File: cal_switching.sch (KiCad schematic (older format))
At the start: 2 parts, among them U20 TMUX6111PWR, U21 TMUX6111PWR

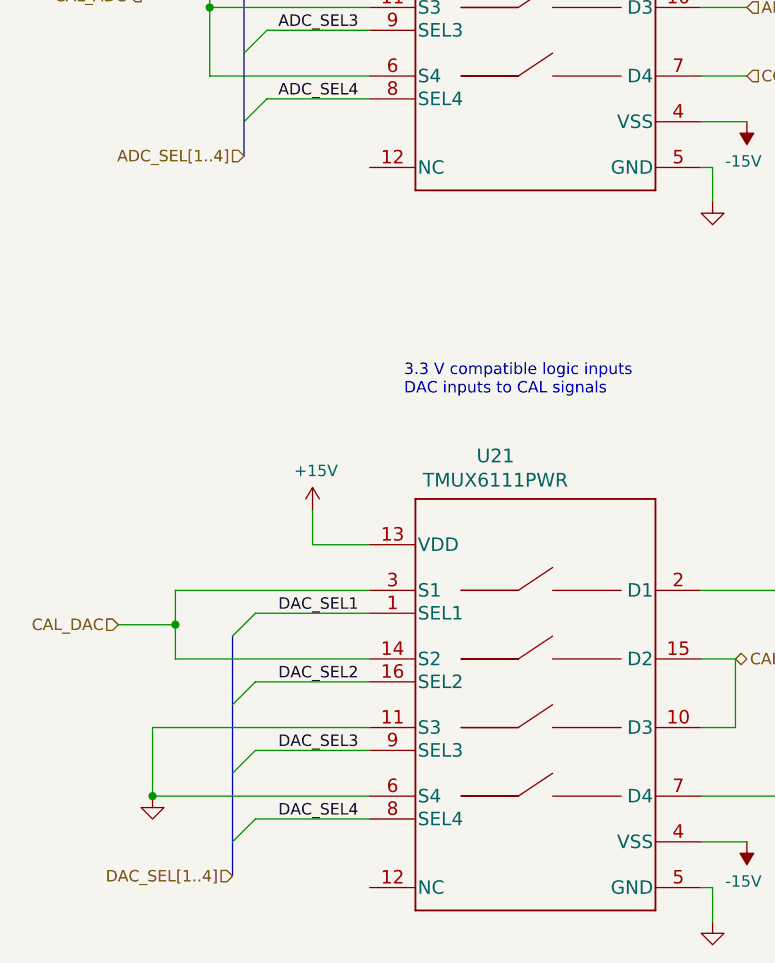
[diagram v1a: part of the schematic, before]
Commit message: reduced ERC to just 4 warnings
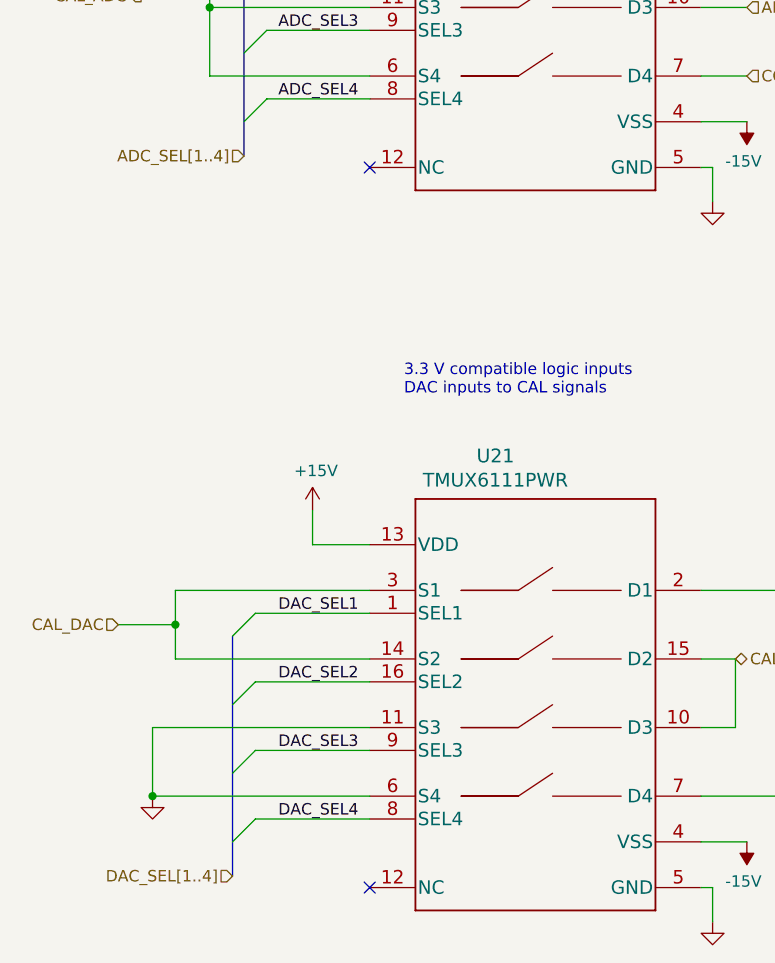
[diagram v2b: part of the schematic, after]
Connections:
- no-connect marks 0 -> 2
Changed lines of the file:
@@
 $Descr A4 11693 8268
 encoding utf-8
-Sheet 5 6
+Sheet 4 6
 Title ""
 Date ""
@@
 Connection ~ 4150 4800
 Connection ~ 4050 5550
+NoConn ~ 5000 5950
+NoConn ~ 5000 2800
 Wire Bus Line
 	4450 1700 4450 2750

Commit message: updates to pcb layout
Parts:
- U20, U21: footprint digikey-footprints:TSSOP-14_W4.4mm -> Package_SO:TSSOP-16_4.4x5mm_P0.65mm
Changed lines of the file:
@@
 F 0 "U20" H 5550 3088 60  0000 C CNN
 F 1 "TMUX6111PWR" H 5550 2982 60  0000 C CNN
-F 2 "digikey-footprints:TSSOP-14_W4.4mm" H 5550 1940 60  0001 C CNN
+F 2 "Package_SO:TSSOP-16_4.4x5mm_P0.65mm" H 5550 1940 60  0001 C CNN
 F 3 "" H 5550 2000 60  0001 C CNN
 F 4 "TMUX6111PWR" H 5550 2000 50  0001 C CNN "Manf#"
@@
 F 0 "U21" H 5550 6238 60  0000 C CNN
 F 1 "TMUX6111PWR" H 5550 6132 60  0000 C CNN
-F 2 "digikey-footprints:TSSOP-14_W4.4mm" H 5550 5090 60  0001 C CNN
+F 2 "Package_SO:TSSOP-16_4.4x5mm_P0.65mm" H 5550 5090 60  0001 C CNN
 F 3 "" H 5550 5150 60  0001 C CNN
 F 4 "TMUX6111PWR" H 5550 5150 50  0001 C CNN "Manf#"

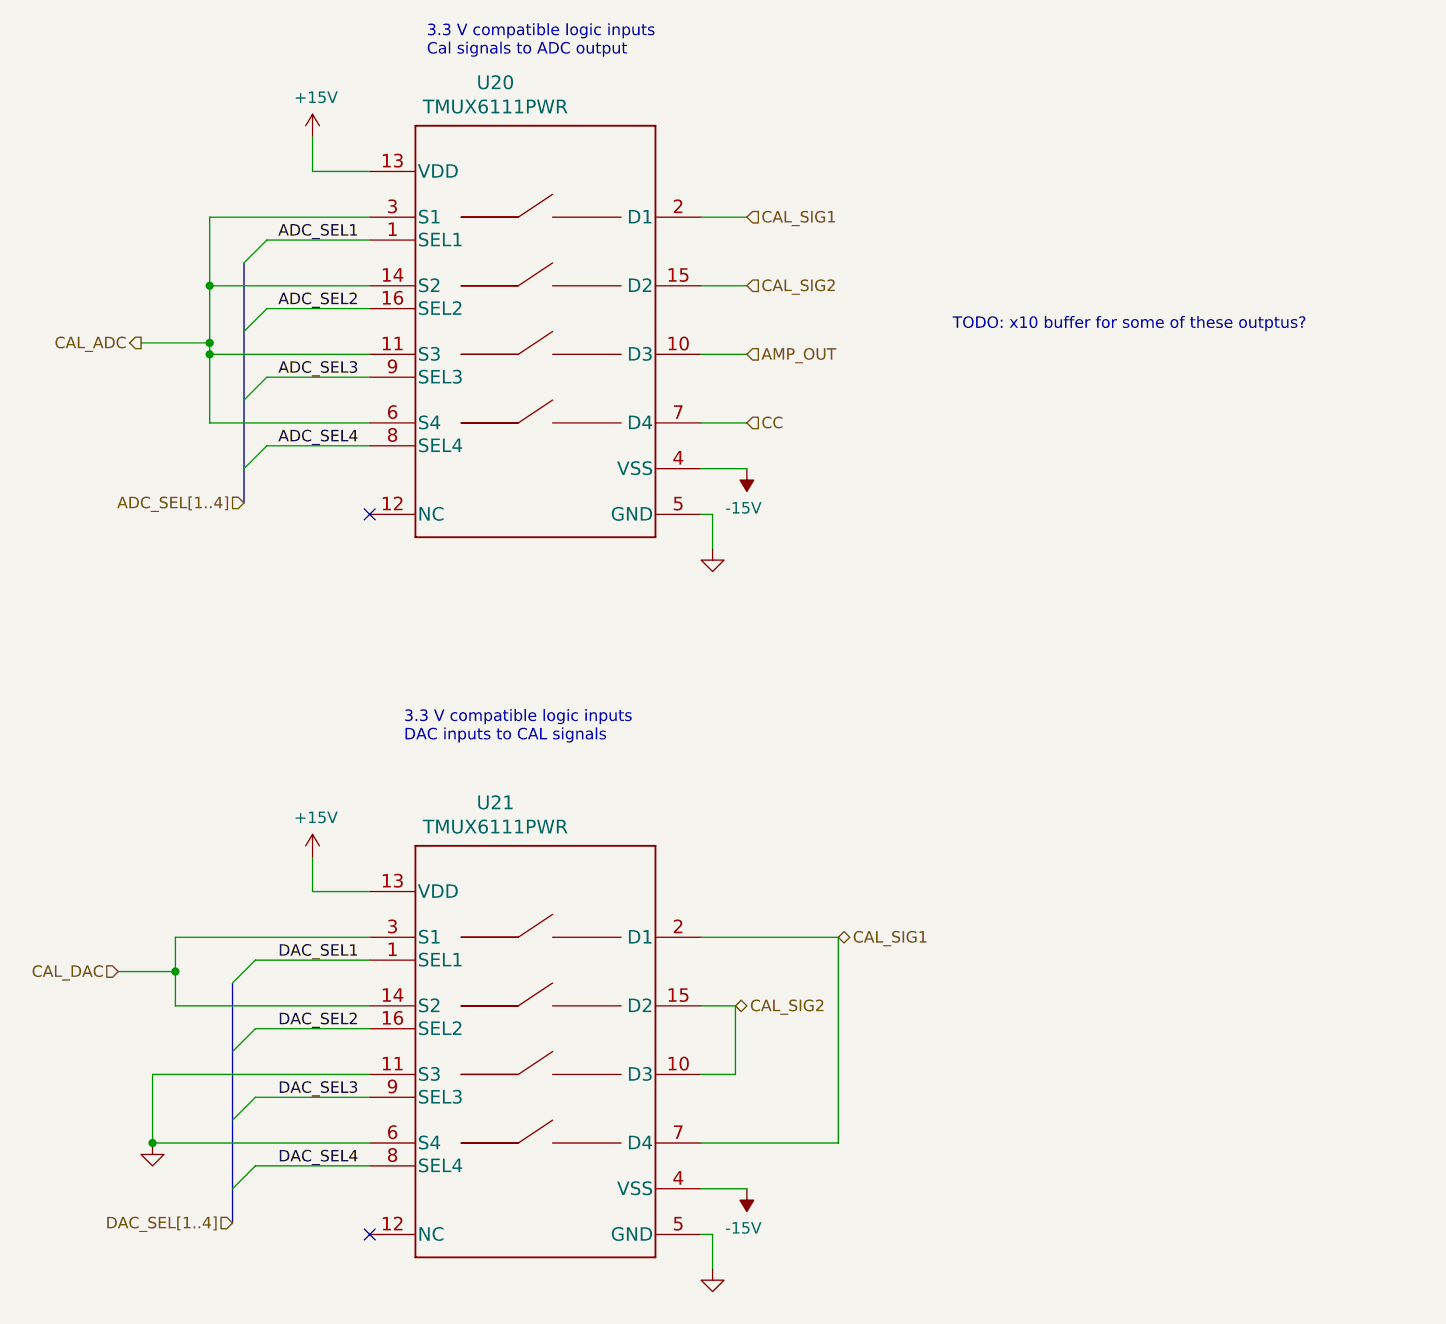
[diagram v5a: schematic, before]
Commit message: updates to README
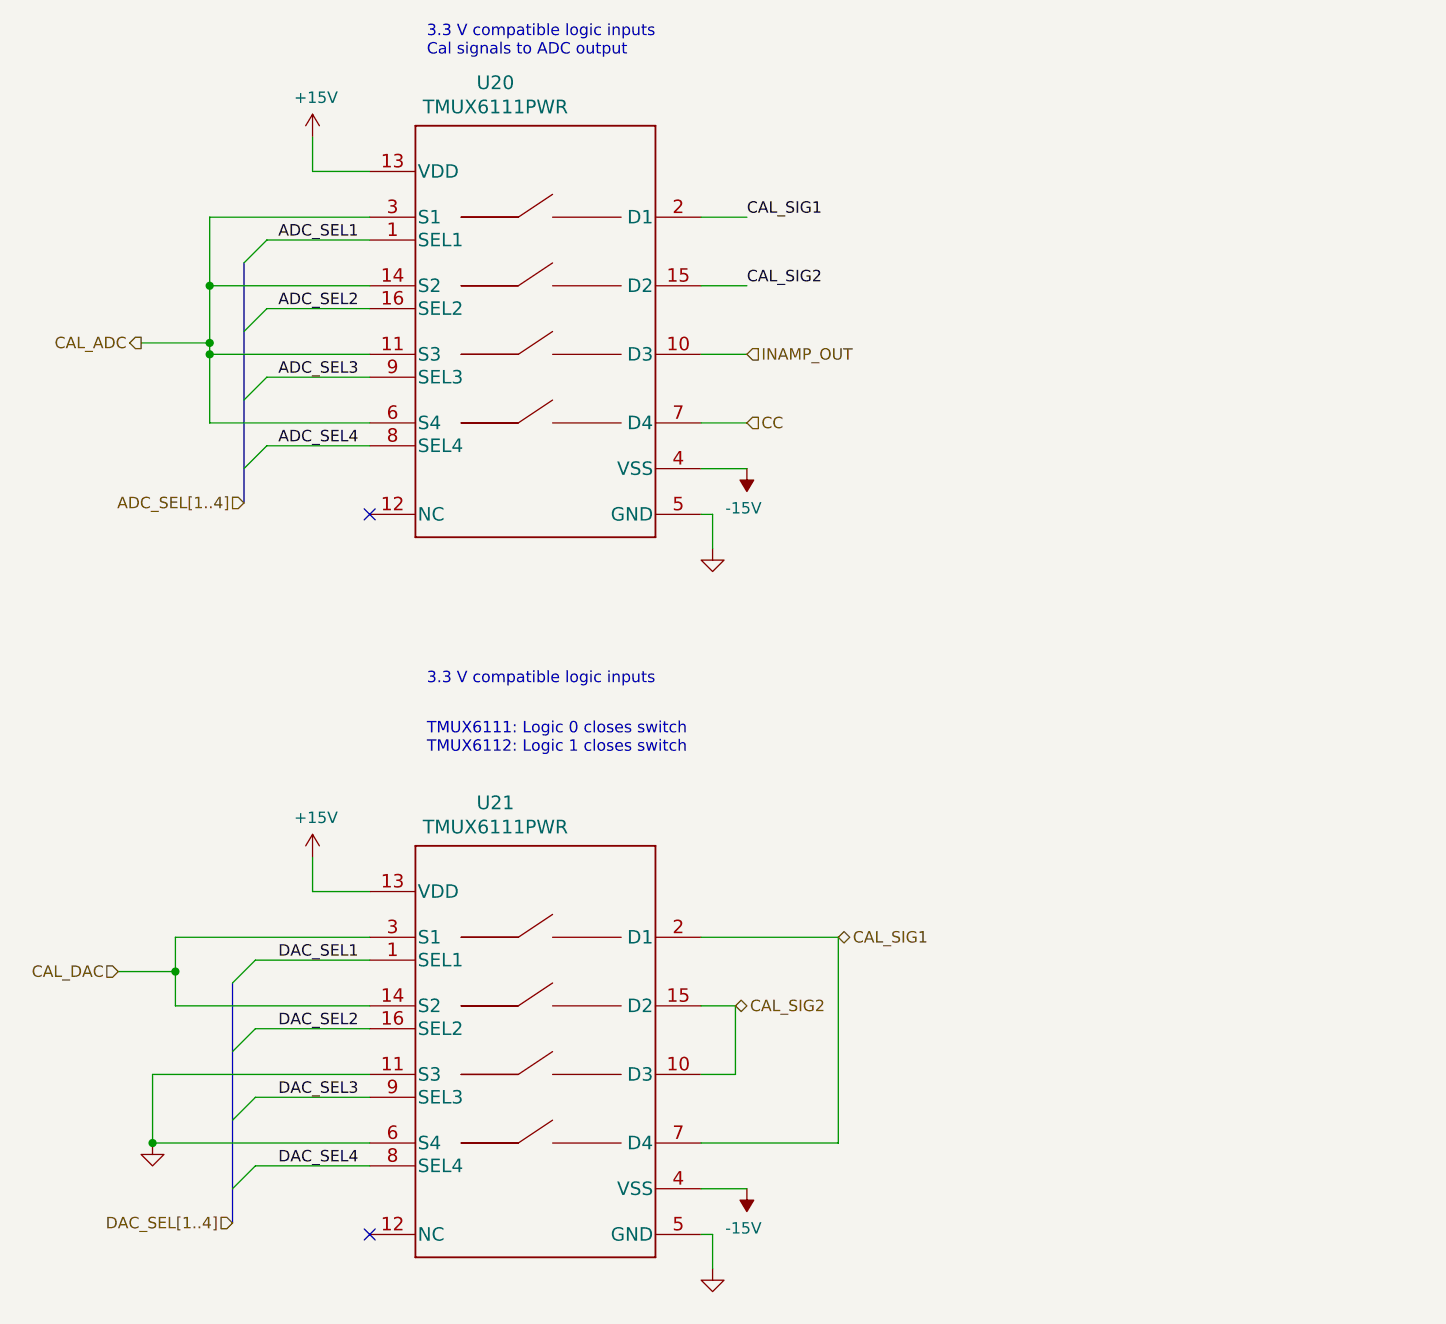
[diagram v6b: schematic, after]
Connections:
- net AMP_OUT renamed INAMP_OUT
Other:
- note added: "3.3 V compatible logic inputs \nDAC inputs or GND to CAL signals"
- note added: "TMUX6111: Logic 0 closes switch\nTMUX6112: Logic 1 closes switch"
- note removed: "3.3 V compatible logic inputs\nDAC inputs to CAL signals"
- note removed: "TODO: x10 buffer for some of these outptus? \n"
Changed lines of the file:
@@
 Text HLabel 4000 2050 0    50   Output ~ 0
 CAL_ADC
-Text HLabel 6650 1500 2    50   Input ~ 0
-CAL_SIG1
 Text Label 4600 1600 0    50   ~ 0
 ADC_SEL1
@@
 Text Label 4600 5650 0    50   ~ 0
 DAC_SEL4
-Text Notes 5150 3800 0    50   ~ 0
-3.3 V compatible logic inputs\nDAC inputs to CAL signals
+Text Notes 5250 3550 0    50   ~ 0
+3.3 V compatible logic inputs \nDAC inputs or GND to CAL signals
 Text HLabel 6600 4950 2    50   BiDi ~ 0
 CAL_SIG2
-Text HLabel 6650 1800 2    50   Input ~ 0
-CAL_SIG2
 Text HLabel 6650 2100 2    50   Input ~ 0
-AMP_OUT
+INAMP_OUT
 Text HLabel 6650 2400 2    50   Input ~ 0
 CC
-Text Notes 7550 2000 0    50   ~ 0
-TODO: x10 buffer for some of these outptus? \n
 Wire Wire Line
 	4750 1150 4750 1300
@@
 Wire Bus Line
 	4400 4850 4400 5900
+Text Label 6650 1500 0    50   ~ 0
+CAL_SIG1
+Text Label 6650 1800 0    50   ~ 0
+CAL_SIG2
+Text Notes 5250 3850 0    50   ~ 0
+TMUX6111: Logic 0 closes switch\nTMUX6112: Logic 1 closes switch
 $EndSCHEMATC

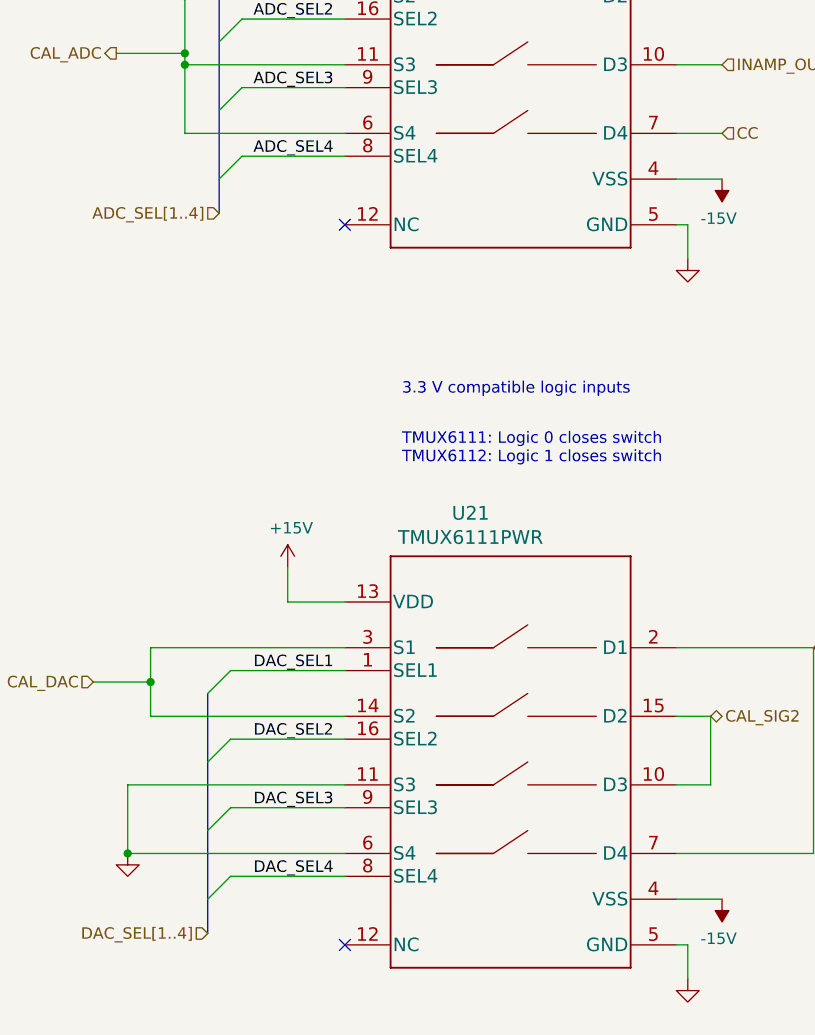
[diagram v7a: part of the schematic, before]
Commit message: added many alternate manufacturing part numbers
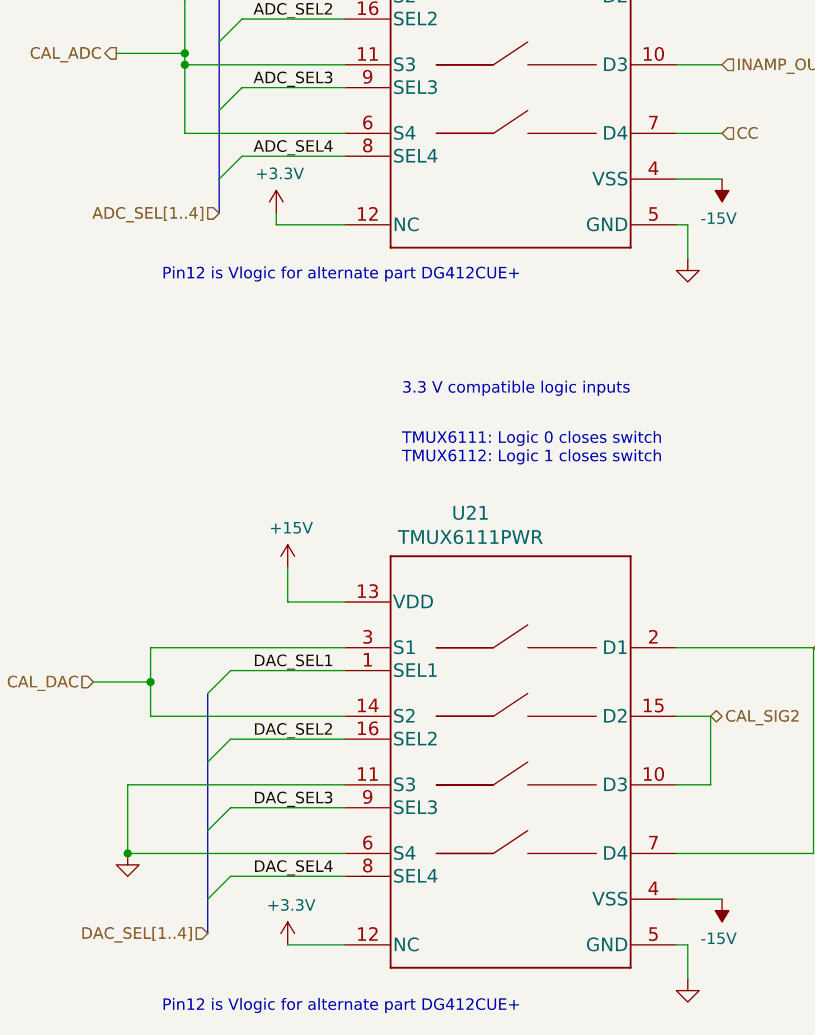
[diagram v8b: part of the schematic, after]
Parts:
- U20: Alternate Manf# (none) -> TMUX6112PWR; Alternate2 Manf# (none) -> DG412CUE+
- U21: Alternate Manf# (none) -> TMUX6112PWR; Alternate2 Manf# (none) -> TMUX6113PWR
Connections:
- net +3V3: now reaches U20.12 (NC)
- net +3V3: now also U21.12 (NC)
- no-connect marks 2 -> 0
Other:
- note added: "Pin12 is Vlogic for alternate part DG412CUE+"
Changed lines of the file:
@@
 F 3 "" H 5550 2000 60  0001 C CNN
 F 4 "TMUX6111PWR" H 5550 2000 50  0001 C CNN "Manf#"
+F 5 "TMUX6112PWR" H 5550 2000 50  0001 C CNN "Alternate Manf#"
+F 6 "DG412CUE+" H 5550 2000 50  0001 C CNN "Alternate2 Manf#"
 	1    5550 2000
 	1    0    0    -1
@@
 F 3 "" H 5550 5150 60  0001 C CNN
 F 4 "TMUX6111PWR" H 5550 5150 50  0001 C CNN "Manf#"
+F 5 "TMUX6112PWR" H 5550 5150 50  0001 C CNN "Alternate Manf#"
+F 6 "TMUX6113PWR" H 5550 5150 50  0001 C CNN "Alternate2 Manf#"
 	1    5550 5150
 	1    0    0    -1
@@
 Connection ~ 4150 4800
 Connection ~ 4050 5550
-NoConn ~ 5000 5950
-NoConn ~ 5000 2800
 Text Label 6650 1500 0    50   ~ 0
 CAL_SIG1
@@
 Text Notes 5250 3850 0    50   ~ 0
 TMUX6111: Logic 0 closes switch\nTMUX6112: Logic 1 closes switch
+$Comp
+L power:+3.3V #PWR?
+U 1 1 6263D73F
+P 4750 5950
+F 0 "#PWR?" H 4750 5800 50  0001 C CNN
+F 1 "+3.3V" H 4765 6123 50  0000 C CNN
+F 2 "" H 4750 5950 50  0001 C CNN
+F 3 "" H 4750 5950 50  0001 C CNN
+	1    4750 5950
+	1    0    0    -1
+$EndComp
+Wire Wire Line
+	4750 5950 5000 5950
+Text Notes 4200 6250 0    50   ~ 0
+Pin12 is Vlogic for alternate part DG412CUE+
+$Comp
+L power:+3.3V #PWR?
+U 1 1 62642C9C
+P 4700 2750
+F 0 "#PWR?" H 4700 2600 50  0001 C CNN
+F 1 "+3.3V" H 4715 2923 50  0000 C CNN
+F 2 "" H 4700 2750 50  0001 C CNN
+F 3 "" H 4700 2750 50  0001 C CNN
+	1    4700 2750
+	1    0    0    -1
+$EndComp
+Wire Wire Line
+	4700 2750 4700 2800
+Wire Wire Line
+	4700 2800 5000 2800
 Wire Bus Line
 	4450 1700 4450 2750
 Wire Bus Line
 	4400 4850 4400 5900
+Text Notes 4200 3050 0    50   ~ 0
+Pin12 is Vlogic for alternate part DG412CUE+
 $EndSCHEMATC
